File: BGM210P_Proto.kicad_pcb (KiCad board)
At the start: 2 copper layers, 58.8 x 43 mm, 39 parts, among them J1 HOST_INTERFACE_CONN, J2 MINI_SIMPLICITY_DEBUG_CONN, J3 HEADER_LEFT, J4 HEADER_RIGHT, J5 SMA_EDGE, SW1 RESET, U1 MIC5504-3.3YM5, U2 BGM210P

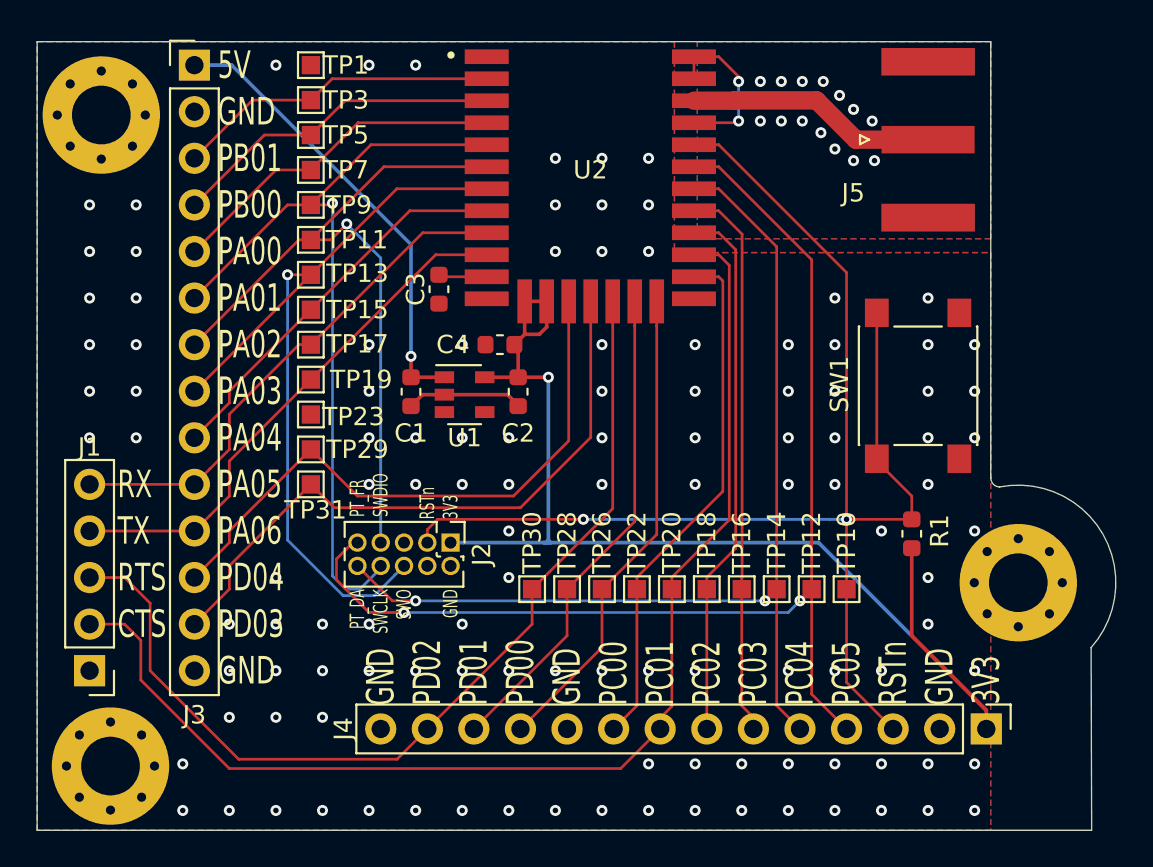
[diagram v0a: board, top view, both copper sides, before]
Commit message: Changed track size from 0.15 to 0.16, added silkscreen artwork , generated fab outputs
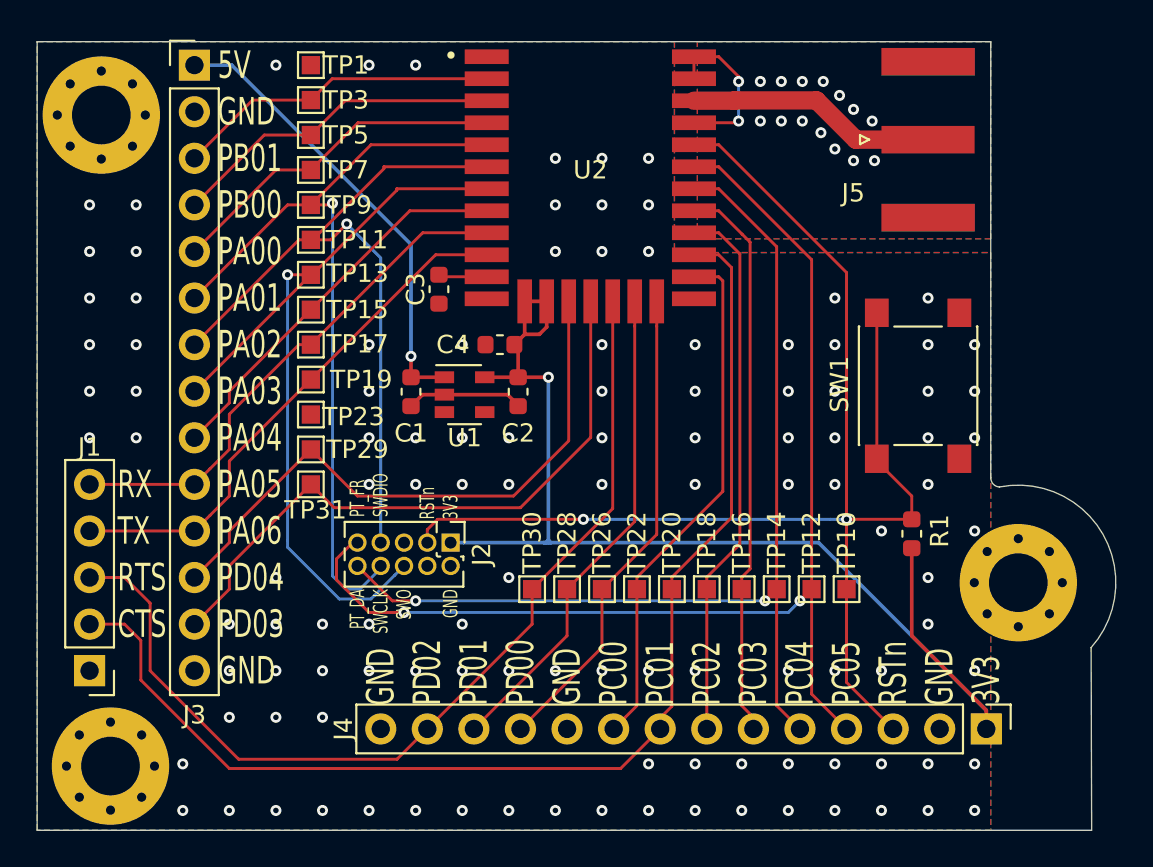
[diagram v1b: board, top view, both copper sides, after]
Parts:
- added G***: LOGO, BGM210P_Proto:MADASS_Logo, F.Cu at (177.1, 100.9)
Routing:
- net GND: vias 117 -> 116
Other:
- net class Default: trace_width 0.15 -> 0.16
- rule trace_min: 0.15 -> 0.16
